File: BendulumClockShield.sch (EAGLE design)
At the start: 24 parts, among them J1 Cold Start, P1 Clock, P2 IR Recv, P3 Coil, P4 Batt, P5 Pwr, U1 LP2951-N

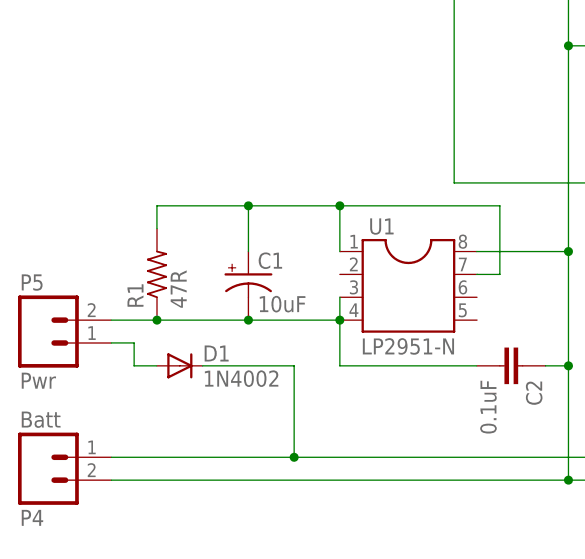
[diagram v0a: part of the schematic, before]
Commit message: Update to Rev G
Increase current drive to 68mA; 42mA for the Arduino and 26mA to keep
the the battery pack fully charged. (26mA is 0.01C for 2500mAh
batteries.)
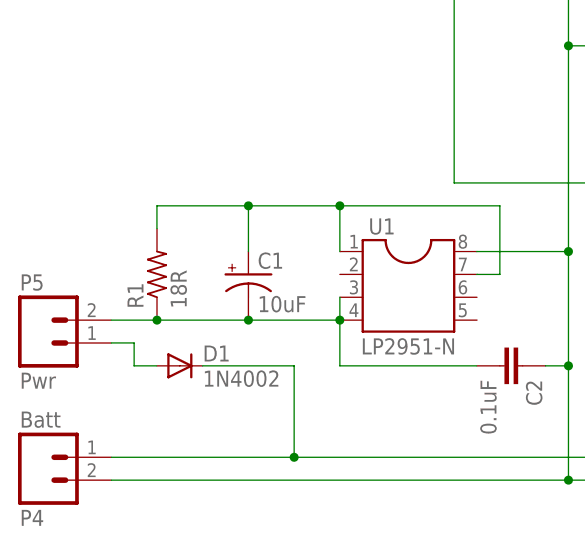
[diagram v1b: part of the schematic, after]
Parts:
- C2: device SparkFun-Capacitors:CAPPTH -> SparkFun-Capacitors:CAPPTH1
- R1: value 47R -> 18R
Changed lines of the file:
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@@
 <part name="D1" library="SparkFun-DiscreteSemi" deviceset="DIODE" device="" value="1N4002"/>
 <part name="C1" library="SparkFun-Capacitors" deviceset="10UF-25V-20%(PTH)" device="" value="10uF"/>
-<part name="C2" library="SparkFun-Capacitors" deviceset="CAP" device="PTH" value="0.1uF"/>
+<part name="C2" library="SparkFun-Capacitors" deviceset="CAP" device="PTH1" value="0.1uF"/>
 <part name="P2" library="dehne" deviceset="M03" device="PTH" value="IR Recv"/>
 <part name="C3" library="SparkFun-Capacitors" deviceset="10UF-25V-20%(PTH)" device="" value="47uF"/>
@@
 <part name="U$1" library="dehne" deviceset="ARDUINO-SHIELD" device=""/>
 <part name="S1" library="dehne" deviceset="TAC_SWITCH" device="PTH" value="Reset"/>
-<part name="R1" library="dehne" deviceset="R-US_" device="" value="47R"/>
+<part name="R1" library="dehne" deviceset="R-US_" device="" value="18R"/>
 <part name="R3" library="dehne" deviceset="R-US_" device="" value="1k"/>
 <part name="R4" library="dehne" deviceset="R-US_" device="" value="47k"/>

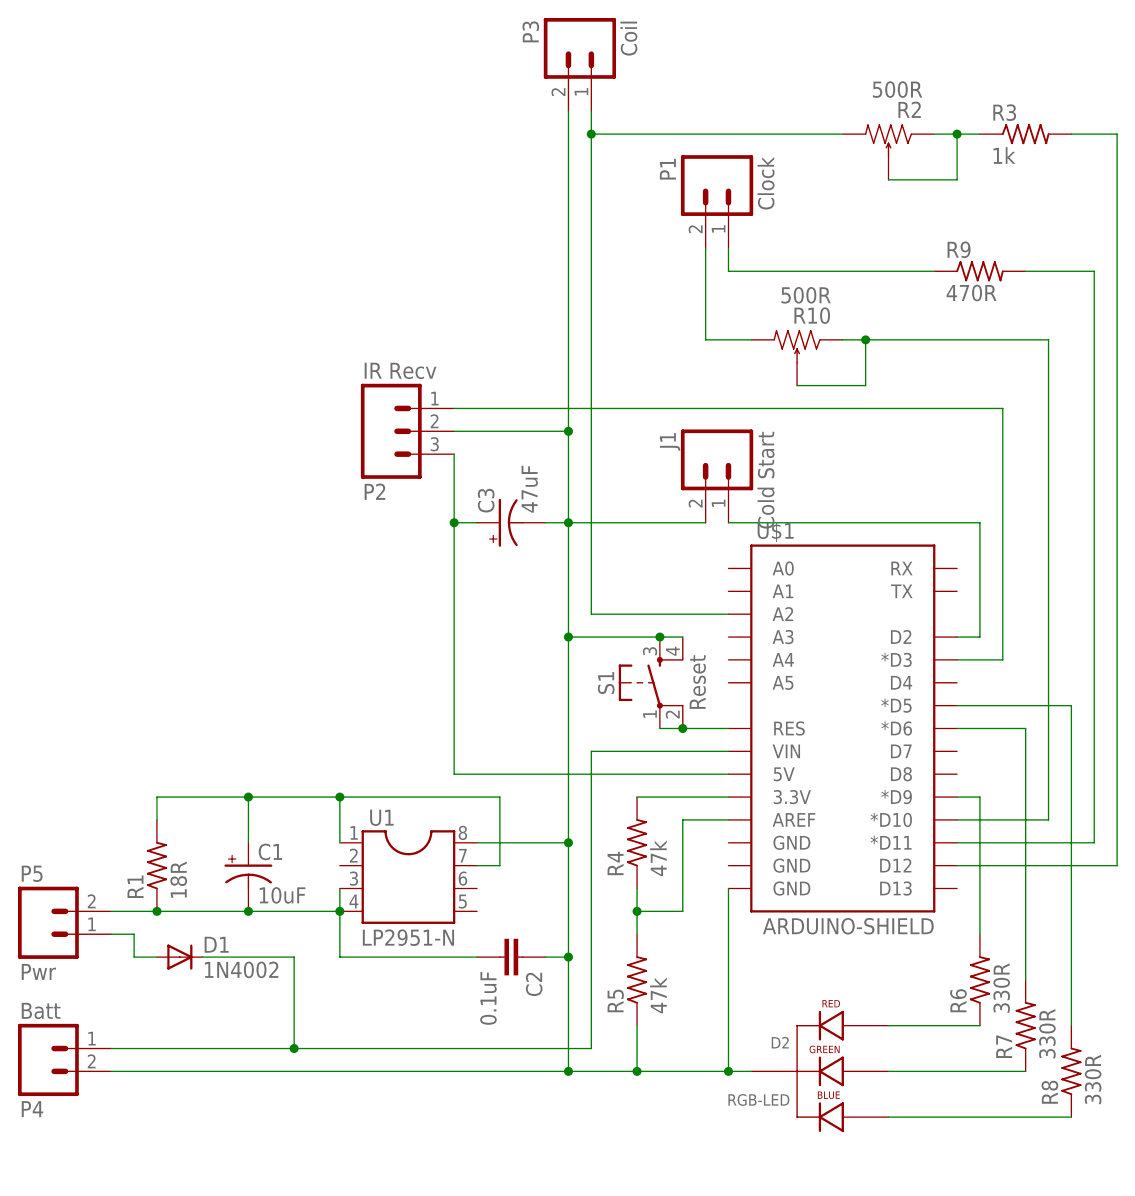
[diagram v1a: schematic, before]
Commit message: Update to Rev H
Add header for TMP-102 temperature sensor
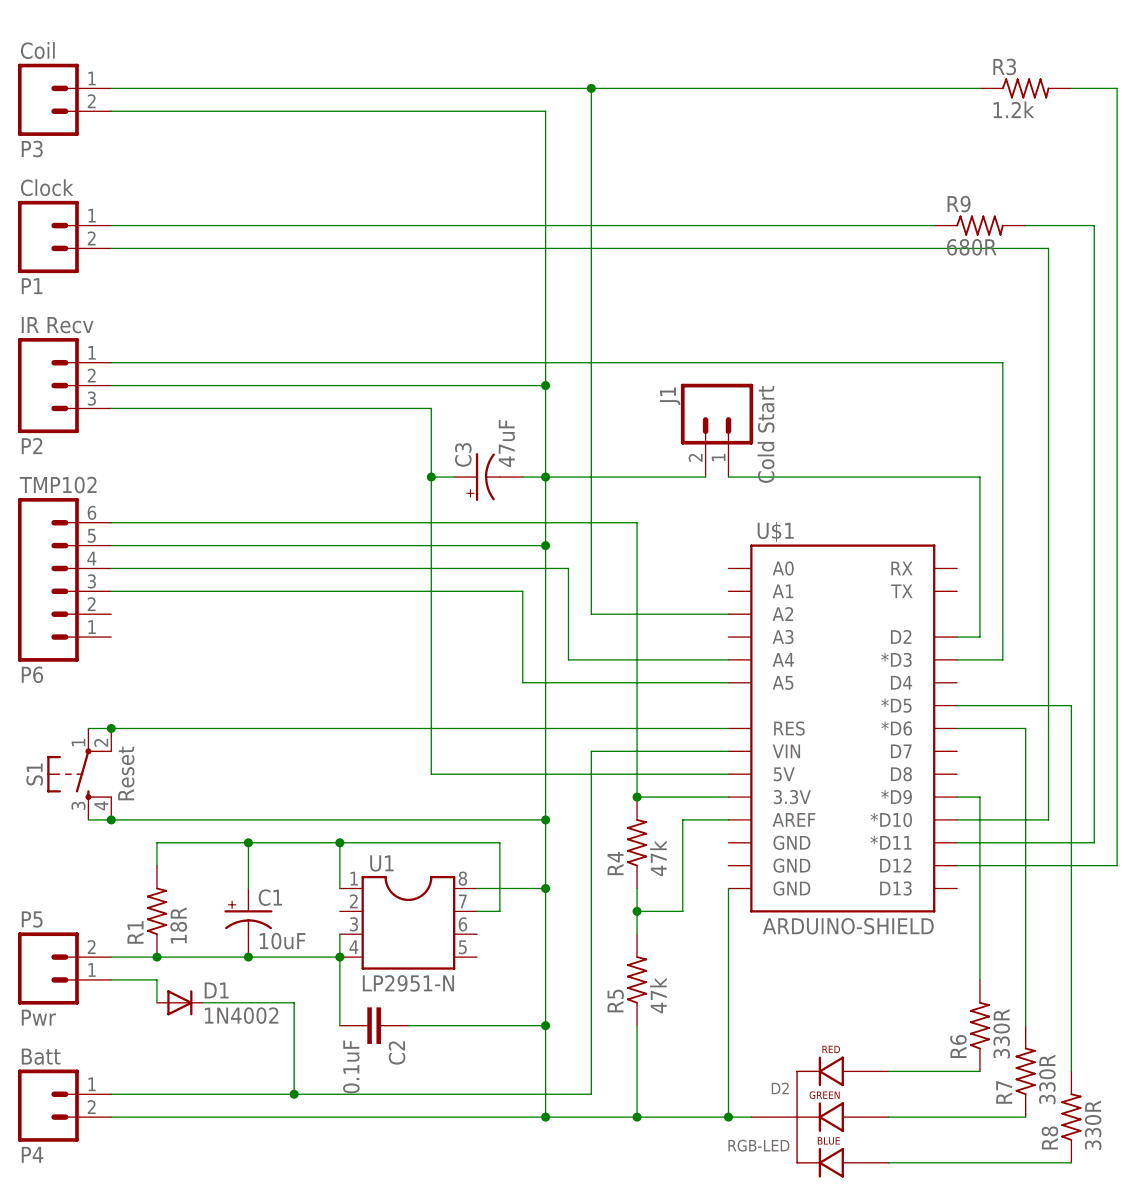
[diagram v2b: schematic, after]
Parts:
- removed R10, R2: 500R, dehne:POTENTIOMETER
- added TMP102: P6, dehne:M06SIP
- R3: value 1k -> 1.2k
- R9: value 470R -> 680R
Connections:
- removed net N$20: P1.2, R10.3
- new net N$16: TMP102.3, U$1.A5
- net GND: now also TMP102.5
- net N$21: now also P1.2; no longer R10.1, R10.2
- net N$6: now also R3.1; no longer R2.3
- net N$7: now also TMP102.6
- net N$9: now also TMP102.4, U$1.A4; no longer R2.1, R2.2, R3.1
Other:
- moved on the sheet: C1, C2, C3, D1, D2, J1, P1, P2, P3, P4, P5, R1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
